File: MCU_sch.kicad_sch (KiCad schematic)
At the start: 20 parts, among them IC3 ATSAMS70N20A-AN, Y3 12MHz

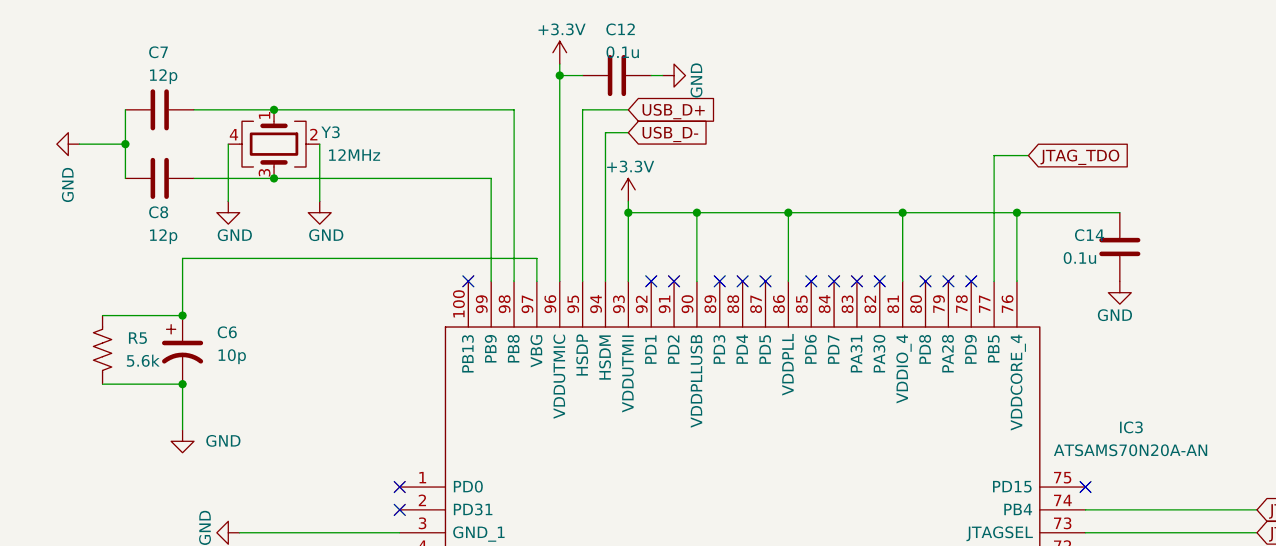
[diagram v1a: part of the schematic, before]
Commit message: Adding part numbers for passives
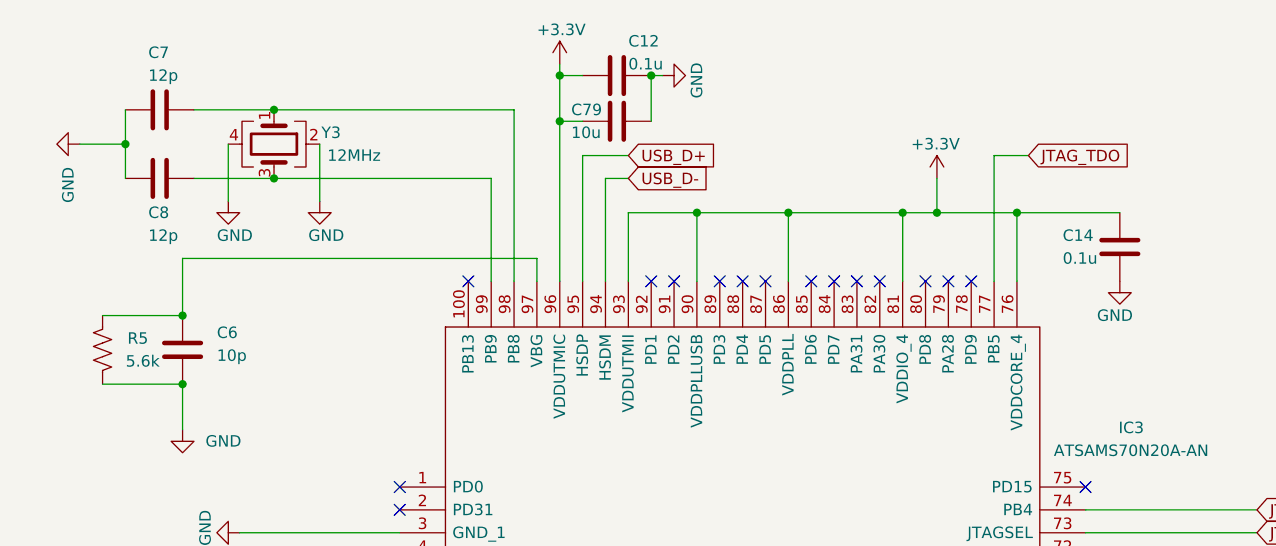
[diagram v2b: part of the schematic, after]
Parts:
- added C79: 10u, Capacitor_SMD:C_0805_2012Metric_Pad1.18x1.45mm_HandSolder, symbol Device:C
- C10, C11, C12, C13, C14, C15, C9: Mouser Part Number (none) -> 187-CL21B104KBCNFNC; Part Number (none) -> CL21B104KBCNFNC
- C6: symbol Device:C_Polarized_US -> Device:C; Mouser Part Number (none) -> 77-VJ0805A100GXJCBC; Part Number (none) -> VJ0805A100GXJCW1BC
- C7, C8: Mouser Part Number (none) -> 80-C0805C120J8G; Part Number (none) -> C0805C120J8GACTU
- D2: Mouser Part Number (none) -> 749-SM0805PGC; Part Number (none) -> SM0805PGC
- R10, R8, R9: Mouser Part Number (none) -> 667-ERJ-P06J472V; Part Number (none) -> ERJ-P06J472V
- R4: Mouser Part Number (none) -> 652-CMP0805-FX-3300L; Part Number (none) -> CMP0805-FX-3300ELF
- R5: Mouser Part Number (none) -> 71-CRCW08055K62FKEAC; Part Number (none) -> CRCW08055K62FKEAC
- Y3: Mouser Part Number (none) -> 815-ABM3B12MHZ12N2YT; Mouser Part number 815-ABM3B12MHZ12N2YT -> (none)
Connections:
- net +3V3: now also C79.2
- net GND: now also C79.1

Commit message: Updating stuff
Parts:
- R5: value 5.6k -> 5.62k
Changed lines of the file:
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@@
       (effects (font (size 1.27 1.27)) (justify left))
     )
-    (property "Value" "5.6k" (id 1) (at 81.28 50.8 0)
+    (property "Value" "5.62k" (id 1) (at 81.28 50.8 0)
       (effects (font (size 1.27 1.27)) (justify left))
     )
